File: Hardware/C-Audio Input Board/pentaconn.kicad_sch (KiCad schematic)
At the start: 8 parts, among them J33 3.5mm, J34 +, J35 -, J36 GND, J37 +_sw, J38 -_sw, J39 Conn_01x05_Socket, J40 Conn_01x03_Socket

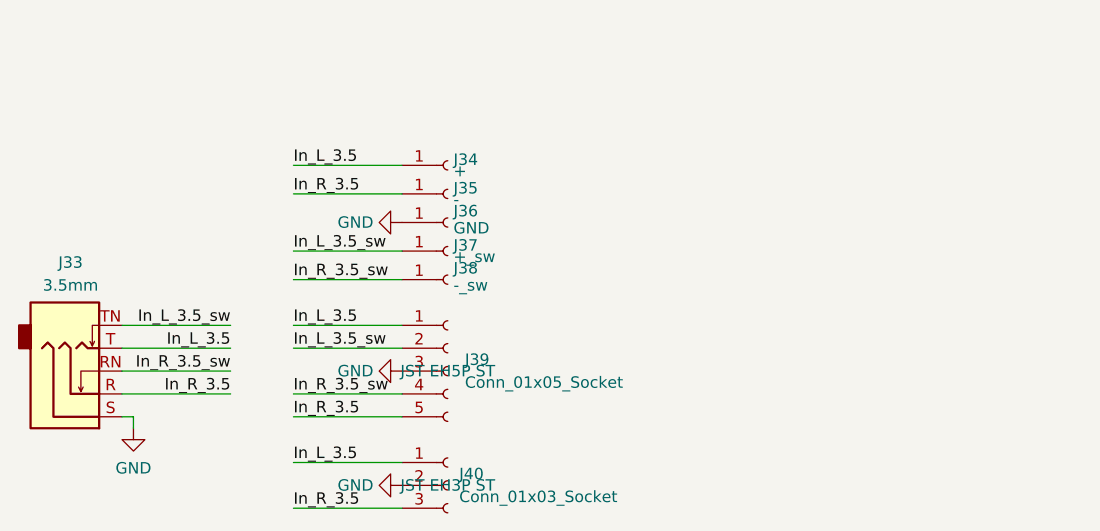
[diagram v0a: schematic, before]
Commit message: added pentaconn and silkscreen marking. Also added PCBWay logo for sponsorship
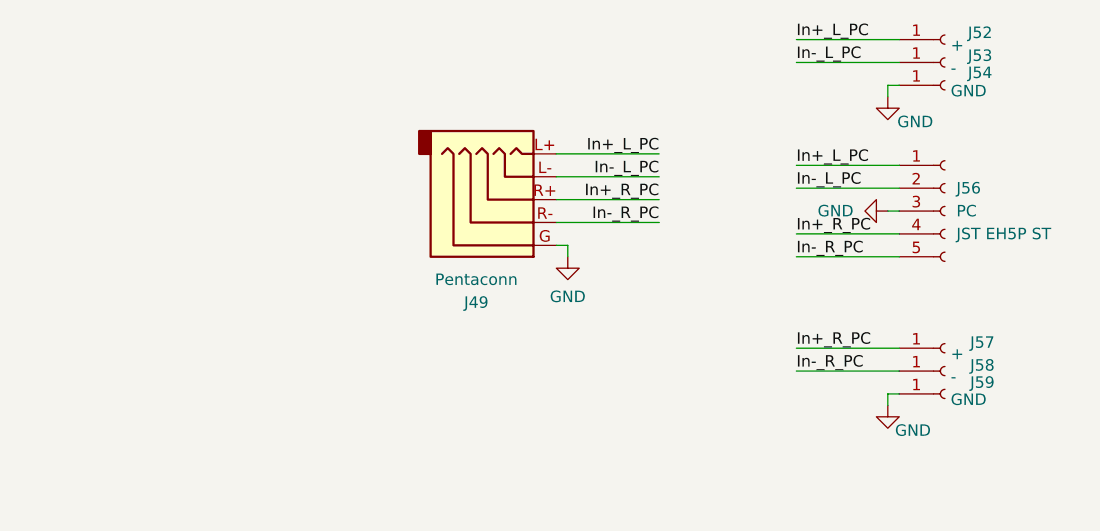
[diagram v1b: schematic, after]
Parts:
- removed J33: 3.5mm, Connector_Audio:Jack_3.5mm_Ledino_KB3SPRS_Horizontal, symbol Connector_Audio:AudioJack3_SwitchTR
- removed J34: +, Connector_Pin:Pin_D1.3mm_L11.0mm, symbol Connector:Conn_01x01_Socket
- removed J35: -, Connector_Pin:Pin_D1.3mm_L11.0mm, symbol Connector:Conn_01x01_Socket
- removed J36: GND, Connector_Pin:Pin_D1.3mm_L11.0mm, symbol Connector:Conn_01x01_Socket
- removed J37: +_sw, Connector_Pin:Pin_D1.3mm_L11.0mm, symbol Connector:Conn_01x01_Socket
- removed J38: -_sw, Connector_Pin:Pin_D1.3mm_L11.0mm, symbol Connector:Conn_01x01_Socket
- removed J39: Conn_01x05_Socket, Connector_JST:JST_EH_B5B-EH-A_1x05_P2.50mm_Vertical, symbol Connector:Conn_01x05_Socket
- removed J40: Conn_01x03_Socket, Connector_JST:JST_EH_B3B-EH-A_1x03_P2.50mm_Vertical, symbol Connector:Conn_01x03_Socket
- added J49: Pentaconn, Connectors Audio Chinch:Pentaconn, symbol Connector_Audio:AudioJack5
- added J52, J57: +, Connector_Pin:Pin_D1.3mm_L11.0mm, symbol Connector:Conn_01x01_Socket
- added J53, J58: -, Connector_Pin:Pin_D1.3mm_L11.0mm, symbol Connector:Conn_01x01_Socket
- added J54, J59: GND, Connector_Pin:Pin_D1.3mm_L11.0mm, symbol Connector:Conn_01x01_Socket
- added J56: PC, Connector_JST:JST_EH_B5B-EH-A_1x05_P2.50mm_Vertical, symbol Connector:Conn_01x05_Socket
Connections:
- net GND: now also J49.G, J54.1 (Pin_1), J56.3 (Pin_3), J59.1 (Pin_1)
- new net In+_L_PC: J49.L+, J52.1 (Pin_1), J56.1 (Pin_1)
- new net In+_R_PC: J49.R+, J56.4 (Pin_4), J57.1 (Pin_1)
- new net In-_L_PC: J49.L-, J53.1 (Pin_1), J56.2 (Pin_2)
- new net In-_R_PC: J49.R-, J56.5 (Pin_5), J58.1 (Pin_1)
